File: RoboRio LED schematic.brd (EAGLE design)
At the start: 100 x 80 mm, 50 parts

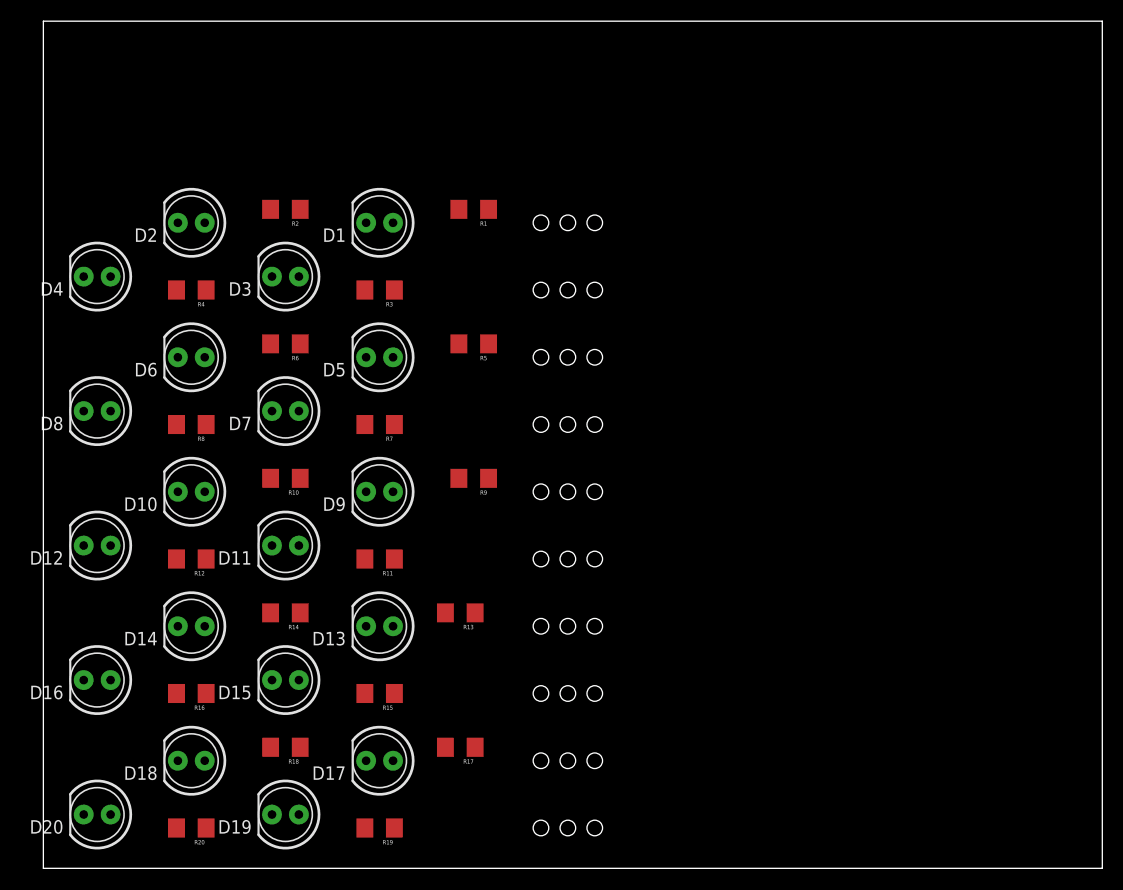
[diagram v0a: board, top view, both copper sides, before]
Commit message: Advanced Electrical Project - Jordan Kiel - Surface Mount RoboRio LED
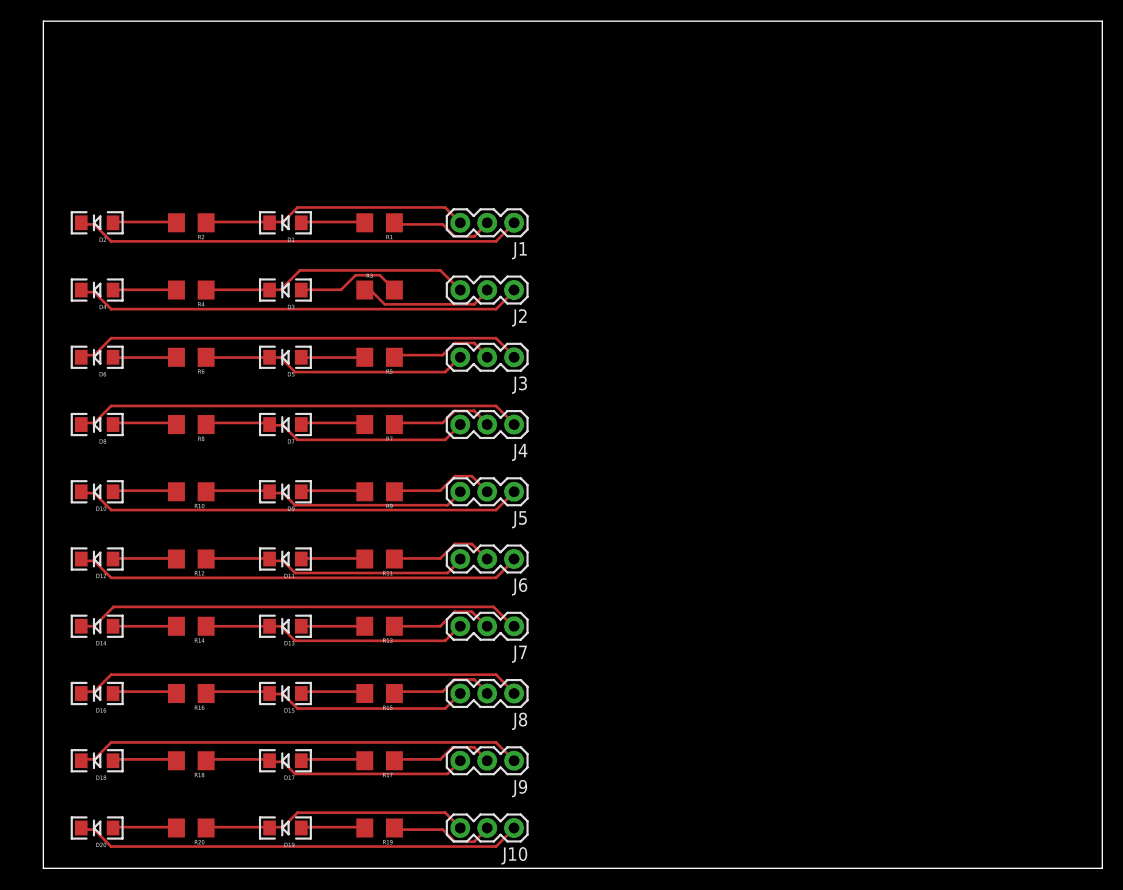
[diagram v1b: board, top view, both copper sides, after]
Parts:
- removed ROBORIO_PWM, ROBORIO_PWM1, ROBORIO_PWM2, ROBORIO_PWM3, ROBORIO_PWM4, ROBORIO_PWM5, ROBORIO_PWM6, ROBORIO_PWM7, ROBORIO_PWM8, ROBORIO_PWM9: (no value), SparkFun-Connectors:1X03_PP_HOLES_ONLY
- added J1, J10, J2, J3, J4, J5, J6, J7, J8, J9: (no value), SparkFun-Connectors:1X03
- D1, D10, D11, D12, D13, D14, D15, D16, D17, D18, D19, D2, D20, D3, D4, D5, D6, D7, D8, D9: device SparkFun-LED:LED5MM -> SparkFun-LED:LED-1206
- moved R5 8.98 mm to (31.8, 48.3)
- moved R1 8.98 mm to (31.8, 61.0)
- moved R14 8.98 mm to (14.0, 22.9)
- moved R18 8.98 mm to (14.0, 10.2)
- moved R6 8.98 mm to (14.0, 48.3)
- moved R9 8.98 mm to (31.8, 35.6)
- moved R10 8.98 mm to (14.0, 35.6)
- moved R2 8.98 mm to (14.0, 61.0)
- moved D1 8.89 mm to (22.9, 61.0)
- moved D10 8.89 mm to (5.08, 35.6)
- moved D13 8.89 mm to (22.9, 22.9)
- moved D14 8.89 mm to (5.08, 22.9)
- moved D17 8.89 mm to (22.9, 10.2)
- moved D18 8.89 mm to (5.08, 10.2)
- moved D2 8.89 mm to (5.08, 61.0)
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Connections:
- net GND: now also D2.C, J1.1; no longer D2.K, ROBORIO_PWM.1
- net GND1: now also D4.C, J2.1; no longer D4.K, ROBORIO_PWM1.1
- net GND2: now also D6.C, J3.1; no longer D6.K, ROBORIO_PWM2.1
- net GND3: now also D8.C, J4.1; no longer D8.K, ROBORIO_PWM3.1
- net GND4: now also D10.C, J5.1; no longer D10.K, ROBORIO_PWM4.1
- net GND5: now also D12.C, J6.1; no longer D12.K, ROBORIO_PWM5.1
- net GND6: now also D14.C, J7.1; no longer D14.K, ROBORIO_PWM6.1
- net GND7: now also D16.C, J8.1; no longer D16.K, ROBORIO_PWM7.1
- net GND8: now also D18.C, J9.1; no longer D18.K, ROBORIO_PWM8.1
- net GND9: now also D20.C, J10.1; no longer D20.K, ROBORIO_PWM9.1
- net N$1: now also J1.2; no longer ROBORIO_PWM.2
- net N$10: now also J4.2; no longer ROBORIO_PWM3.2
- net N$13: now also J5.2; no longer ROBORIO_PWM4.2
- net N$16: now also J6.2; no longer ROBORIO_PWM5.2
- net N$19: now also J7.2; no longer ROBORIO_PWM6.2
- net N$22: now also J8.2; no longer ROBORIO_PWM7.2
- net N$25: now also J9.2; no longer ROBORIO_PWM8.2
- net N$28: now also J10.2; no longer ROBORIO_PWM9.2
- net N$3: now also J2.2; no longer ROBORIO_PWM1.2
- net N$7: now also J3.2; no longer ROBORIO_PWM2.2
- net S: now also D1.C, J1.3; no longer D1.K, ROBORIO_PWM.3
- net S1: now also D3.C, J2.3; no longer D3.K, ROBORIO_PWM1.3
- net S2: now also D5.C, J3.3; no longer D5.K, ROBORIO_PWM2.3
- net S3: now also D7.C, J4.3; no longer D7.K, ROBORIO_PWM3.3
- net S4: now also D9.C, J5.3; no longer D9.K, ROBORIO_PWM4.3
- net S5: now also D11.C, J6.3; no longer D11.K, ROBORIO_PWM5.3
- net S6: now also D13.C, J7.3; no longer D13.K, ROBORIO_PWM6.3
- net S7: now also D15.C, J8.3; no longer D15.K, ROBORIO_PWM7.3
- net S8: now also D17.C, J9.3; no longer D17.K, ROBORIO_PWM8.3
- net S9: now also D19.C, J10.3; no longer D19.K, ROBORIO_PWM9.3
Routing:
- net GND2: track 0.00 -> 42.5 mm
- net GND1: track 0.00 -> 42.5 mm
- net GND5: track 0.00 -> 42.4 mm
- net GND7: track 0.00 -> 42.4 mm
- net GND6: track 0.00 -> 42.4 mm
- net GND9: track 0.00 -> 42.4 mm
- net GND3: track 0.00 -> 42.4 mm
- net GND: track 0.00 -> 42.4 mm
- net GND4: track 0.00 -> 42.3 mm
- net GND8: track 0.00 -> 42.3 mm
- net S1: track 0.00 -> 25.5 mm
- net S7: track 0.00 -> 25.3 mm
- net S3: track 0.00 -> 25.3 mm
- net S: track 0.00 -> 25.2 mm
- net S9: track 0.00 -> 25.2 mm
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
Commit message: Changed placement for one sub-circuit
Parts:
- moved D2 48.3 mm to (53.3, 61.0), turned to 90 degrees
- moved R2 35.6 mm to (49.5, 61.0), turned to 270 degrees
- moved D1 7.62 mm to (30.5, 61.0), turned to 90 degrees
- moved R1 2.54 mm to (34.3, 61.0), turned to 270 degrees
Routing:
- net GND: track 42.4 -> 9.50 mm
- net S: track 25.2 -> 21.2 mm
- net N$4: track 6.04 -> 3.88 mm
- net N$2: track 6.03 -> 3.94 mm
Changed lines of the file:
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@@
 <?xml version="1.0" encoding="utf-8"?>
 <!DOCTYPE eagle SYSTEM "eagle.dtd">
-<eagle version="7.6.0">
+<eagle version="7.1.0">
 <drawing>
 <settings>
@@
 <setting verticaltext="up"/>
 </settings>
-<grid distance="0.05" unitdist="inch" unit="inch" style="lines" multiple="1" display="yes" altdistance="0.025" altunitdist="inch" altunit="inch"/>
+<grid distance="0.1" unitdist="inch" unit="inch" style="lines" multiple="1" display="yes" altdistance="0.025" altunitdist="inch" altunit="inch"/>
 <layers>
 <layer number="1" name="Top" color="4" fill="1" visible="yes" active="yes"/>
@@
 </autorouter>
 <elements>
-<element name="D1" library="SparkFun-LED" package="LED-1206" value="" x="22.86" y="60.96" rot="R180"/>
+<element name="D1" library="SparkFun-LED" package="LED-1206" value="" x="30.48" y="60.96" rot="R90"/>
 <element name="D10" library="SparkFun-LED" package="LED-1206" value="" x="5.08" y="35.56" rot="R180"/>
 <element name="D11" library="SparkFun-LED" package="LED-1206" value="" x="22.86" y="29.21" rot="R180"/>
@@
 <element name="D18" library="SparkFun-LED" package="LED-1206" value="" x="5.08" y="10.16" rot="R180"/>
 <element name="D19" library="SparkFun-LED" package="LED-1206" value="" x="22.86" y="3.81" rot="R180"/>
-<element name="D2" library="SparkFun-LED" package="LED-1206" value="" x="5.08" y="60.96" rot="R180"/>
+<element name="D2" library="SparkFun-LED" package="LED-1206" value="" x="53.34" y="60.96" rot="R90"/>
 <element name="D20" library="SparkFun-LED" package="LED-1206" value="" x="5.08" y="3.81" rot="R180"/>
 <element name="D3" library="SparkFun-LED" package="LED-1206" value="" x="22.86" y="54.61" rot="R180"/>
@@
 <element name="J8" library="SparkFun-Connectors" package="1X03" value="" x="44.45" y="16.51" rot="R180"/>
 <element name="J9" library="SparkFun-Connectors" package="1X03" value="" x="44.45" y="10.16" rot="R180"/>
-<element name="R1" library="SparkFun-Passives" package="1206" value="" x="31.75" y="60.96" rot="R180"/>
+<element name="R1" library="SparkFun-Passives" package="1206" value="" x="34.29" y="60.96" rot="R270"/>
 <element name="R10" library="SparkFun-Passives" package="1206" value="" x="13.97" y="35.56" rot="R180"/>
 <element name="R11" library="SparkFun-Passives" package="1206" value="" x="31.75" y="29.21" rot="R180"/>
@@
 <element name="R18" library="SparkFun-Passives" package="1206" value="" x="13.97" y="10.16" rot="R180"/>
 <element name="R19" library="SparkFun-Passives" package="1206" value="" x="31.75" y="3.81" rot="R180"/>
-<element name="R2" library="SparkFun-Passives" package="1206" value="" x="13.97" y="60.96" rot="R180"/>
+<element name="R2" library="SparkFun-Passives" package="1206" value="" x="49.53" y="60.96" rot="R270"/>
 <element name="R20" library="SparkFun-Passives" package="1206" value="" x="13.97" y="3.81" rot="R180"/>
 <element name="R3" library="SparkFun-Passives" package="1206" value="" x="31.75" y="54.61"/>
@@
 <contactref element="J1" pad="3"/>
 <contactref element="D1" pad="C"/>
-<wire x1="15.5448" y1="61.0362" x2="21.2598" y2="61.0362" width="0.254" layer="1"/>
-<wire x1="21.2598" y1="61.0362" x2="21.36" y2="60.96" width="0.254" layer="1"/>
-<wire x1="15.5448" y1="61.0362" x2="15.37" y2="60.96" width="0.254" layer="1"/>
-<wire x1="22.6314" y1="61.0362" x2="21.4884" y2="61.0362" width="0.254" layer="1"/>
-<wire x1="24.003" y1="62.4078" x2="22.6314" y2="61.0362" width="0.254" layer="1"/>
-<wire x1="37.9476" y1="62.4078" x2="24.003" y2="62.4078" width="0.254" layer="1"/>
-<wire x1="39.3192" y1="61.0362" x2="37.9476" y2="62.4078" width="0.254" layer="1"/>
-<wire x1="21.4884" y1="61.0362" x2="21.36" y2="60.96" width="0.254" layer="1"/>
+<wire x1="32.2326" y1="62.6364" x2="30.6324" y2="62.6364" width="0.254" layer="1"/>
+<wire x1="33.147" y1="63.5508" x2="32.2326" y2="62.6364" width="0.254" layer="1"/>
+<wire x1="36.8046" y1="63.5508" x2="33.147" y2="63.5508" width="0.254" layer="1"/>
+<wire x1="39.3192" y1="61.0362" x2="36.8046" y2="63.5508" width="0.254" layer="1"/>
+<wire x1="30.6324" y1="62.6364" x2="30.48" y2="62.46" width="0.254" layer="1"/>
 <wire x1="39.3192" y1="61.0362" x2="39.37" y2="60.96" width="0.254" layer="1"/>
+<wire x1="40.9194" y1="62.4078" x2="49.3776" y2="62.4078" width="0.254" layer="1"/>
+<wire x1="39.5478" y1="61.0362" x2="40.9194" y2="62.4078" width="0.254" layer="1"/>
+<wire x1="49.3776" y1="62.4078" x2="49.53" y2="62.36" width="0.254" layer="1"/>
+<wire x1="39.5478" y1="61.0362" x2="39.37" y2="60.96" width="0.254" layer="1"/>
 </signal>
 <signal name="GND">
 <contactref element="J1" pad="1"/>
 <contactref element="D2" pad="C"/>
-<wire x1="4.8006" y1="60.8076" x2="3.6576" y2="60.8076" width="0.254" layer="1"/>
-<wire x1="6.4008" y1="59.2074" x2="4.8006" y2="60.8076" width="0.254" layer="1"/>
-<wire x1="42.7482" y1="59.2074" x2="6.4008" y2="59.2074" width="0.254" layer="1"/>
-<wire x1="44.3484" y1="60.8076" x2="42.7482" y2="59.2074" width="0.254" layer="1"/>
-<wire x1="3.6576" y1="60.8076" x2="3.58" y2="60.96" width="0.254" layer="1"/>
-<wire x1="44.3484" y1="60.8076" x2="44.45" y2="60.96" width="0.254" layer="1"/>
+<wire x1="51.8922" y1="62.4078" x2="53.2638" y2="62.4078" width="0.254" layer="1"/>
+<wire x1="50.5206" y1="61.0362" x2="51.8922" y2="62.4078" width="0.254" layer="1"/>
+<wire x1="44.577" y1="61.0362" x2="50.5206" y2="61.0362" width="0.254" layer="1"/>
+<wire x1="53.2638" y1="62.4078" x2="53.34" y2="62.46" width="0.254" layer="1"/>
+<wire x1="44.577" y1="61.0362" x2="44.45" y2="60.96" width="0.254" layer="1"/>
 </signal>
 <signal name="N$1">
 <contactref element="R1" pad="1"/>
 <contactref element="J1" pad="2"/>
-<wire x1="37.719" y1="60.8076" x2="33.3756" y2="60.8076" width="0.254" layer="1"/>
-<wire x1="38.862" y1="59.6646" x2="37.719" y2="60.8076" width="0.254" layer="1"/>
+<wire x1="36.3474" y1="62.1792" x2="34.29" y2="62.1792" width="0.254" layer="1"/>
+<wire x1="38.862" y1="59.6646" x2="36.3474" y2="62.1792" width="0.254" layer="1"/>
 <wire x1="40.6908" y1="59.6646" x2="38.862" y2="59.6646" width="0.254" layer="1"/>
 <wire x1="41.8338" y1="60.8076" x2="40.6908" y2="59.6646" width="0.254" layer="1"/>
-<wire x1="33.3756" y1="60.8076" x2="33.15" y2="60.96" width="0.254" layer="1"/>
+<wire x1="34.29" y1="62.1792" x2="34.29" y2="62.36" width="0.254" layer="1"/>
 <wire x1="41.8338" y1="60.8076" x2="41.91" y2="60.96" width="0.254" layer="1"/>
 </signal>
@@
 <contactref element="R2" pad="2"/>
 <contactref element="D2" pad="A"/>
-<wire x1="12.3444" y1="61.0362" x2="6.6294" y2="61.0362" width="0.254" layer="1"/>
-<wire x1="6.6294" y1="61.0362" x2="6.58" y2="60.96" width="0.254" layer="1"/>
-<wire x1="12.3444" y1="61.0362" x2="12.57" y2="60.96" width="0.254" layer="1"/>
+<wire x1="49.6062" y1="59.436" x2="53.2638" y2="59.436" width="0.254" layer="1"/>
+<wire x1="53.2638" y1="59.436" x2="53.34" y2="59.46" width="0.254" layer="1"/>
+<wire x1="49.6062" y1="59.436" x2="49.53" y2="59.56" width="0.254" layer="1"/>
 </signal>
 <signal name="N$2">
 <contactref element="R1" pad="2"/>
 <contactref element="D1" pad="A"/>
-<wire x1="30.1752" y1="61.0362" x2="24.4602" y2="61.0362" width="0.254" layer="1"/>
-<wire x1="24.4602" y1="61.0362" x2="24.36" y2="60.96" width="0.254" layer="1"/>
-<wire x1="30.1752" y1="61.0362" x2="30.35" y2="60.96" width="0.254" layer="1"/>
+<wire x1="34.29" y1="59.436" x2="30.6324" y2="59.436" width="0.254" layer="1"/>
+<wire x1="30.6324" y1="59.436" x2="30.48" y2="59.46" width="0.254" layer="1"/>
+<wire x1="34.29" y1="59.436" x2="34.29" y2="59.56" width="0.254" layer="1"/>
 </signal>
 <signal name="S1">

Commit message: Trial layouts, smaller components, no need to review
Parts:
- D1, D10, D11, D12, D13, D14, D15, D16, D17, D18, D19, D2, D20, D3, D4, D5, D6, D7, D8, D9: device SparkFun-LED:LED-1206 -> LilyPad-Wearables:LED-1206
- R1, R10, R11, R12, R13, R14, R15, R16, R17, R18, R19, R2, R20, R3, R4, R5, R6, R7, R8, R9: device SparkFun-Passives:1206 -> SparkFun-Passives:0603-RES
- moved D4 84.8 mm to (88.9, 67.3), turned to 270 degrees
- moved D6 84.3 mm to (88.9, 57.1), turned to 270 degrees
- moved D14 84.1 mm to (88.9, 16.5), turned to 90 degrees
- moved D8 84.0 mm to (88.9, 47.0), turned to 270 degrees
- moved D12 83.9 mm to (88.9, 26.7), turned to 270 degrees
- moved D10 83.8 mm to (88.9, 36.8), turned to 270 degrees
- moved R4 77.0 mm to (88.9, 72.4), turned to 270 degrees
- moved R6 76.2 mm to (88.9, 62.2), turned to 270 degrees
- moved R8 75.6 mm to (88.9, 52.1), turned to 270 degrees
- moved R10 75.2 mm to (88.9, 41.9), turned to 270 degrees
- moved R12 75.0 mm to (88.9, 31.8), turned to 270 degrees
- moved D18 69.9 mm to (39.4, 71.1), turned to 0 degrees
- moved D17 68.1 mm to (39.4, 76.2)
- moved R14 67.7 mm to (81.3, 15.2), turned to 270 degrees
- moved R18 67.1 mm to (35.6, 73.7), turned to 270 degrees
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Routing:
- net GND2: track 42.5 -> 0.00 mm
- net GND1: track 42.5 -> 0.00 mm
- net GND5: track 42.4 -> 0.00 mm
- net GND7: track 42.4 -> 0.00 mm
- net GND6: track 42.4 -> 0.00 mm
- net GND9: track 42.4 -> 0.00 mm
- net GND3: track 42.4 -> 0.00 mm
- net GND4: track 42.3 -> 0.00 mm
- net GND8: track 42.3 -> 0.00 mm
- net S1: track 25.5 -> 0.00 mm
- net S7: track 25.3 -> 0.00 mm
- net S3: track 25.3 -> 0.00 mm
- net S9: track 25.2 -> 0.00 mm
- net S5: track 25.2 -> 0.00 mm
- net S4: track 25.2 -> 0.00 mm
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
